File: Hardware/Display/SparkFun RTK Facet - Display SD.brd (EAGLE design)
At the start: 49 x 22 mm, 42 parts, among them J1 FPC_12_0.5MM_BACKFLIP, J2 MICRO-SD-PUSH-PUSH-EXT-PIN, J3 FPC_12_0.5MM_BACKFLIP, U13 LIS2DH12

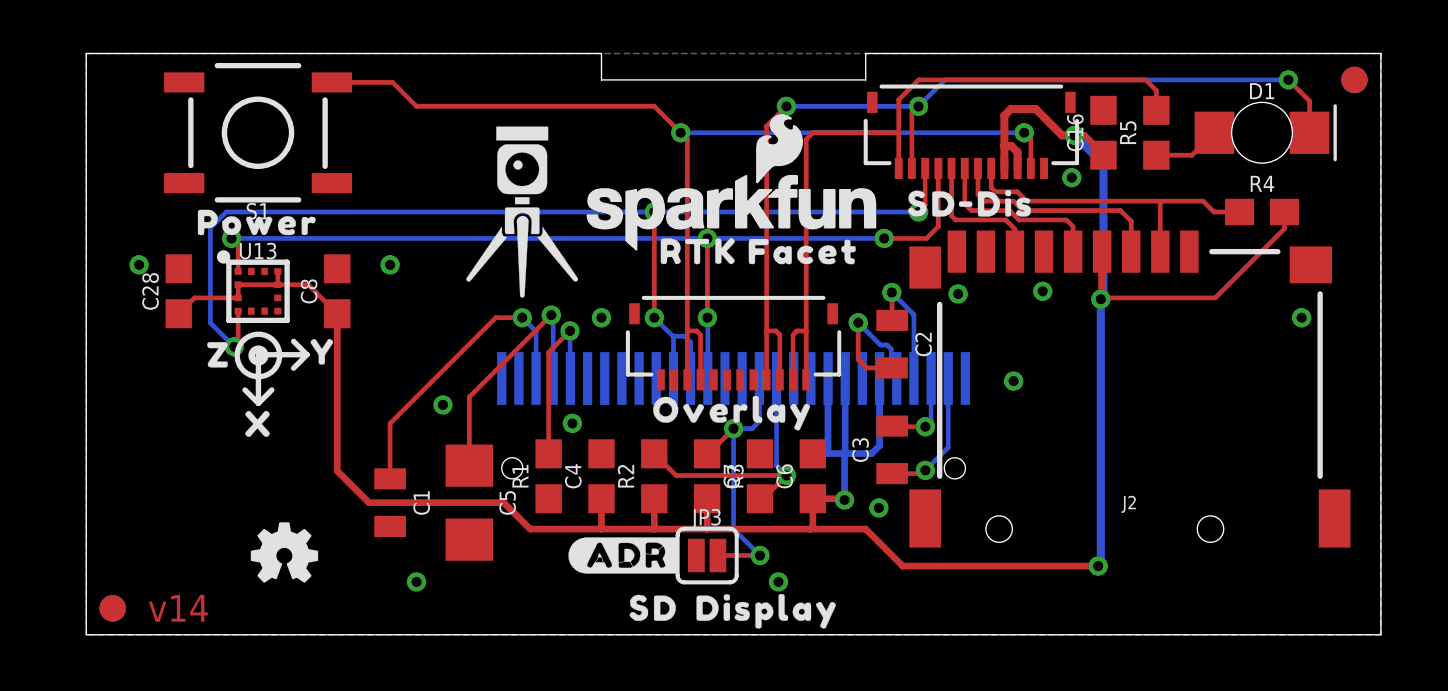
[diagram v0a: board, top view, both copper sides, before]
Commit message: Move to LIF overlay connector.
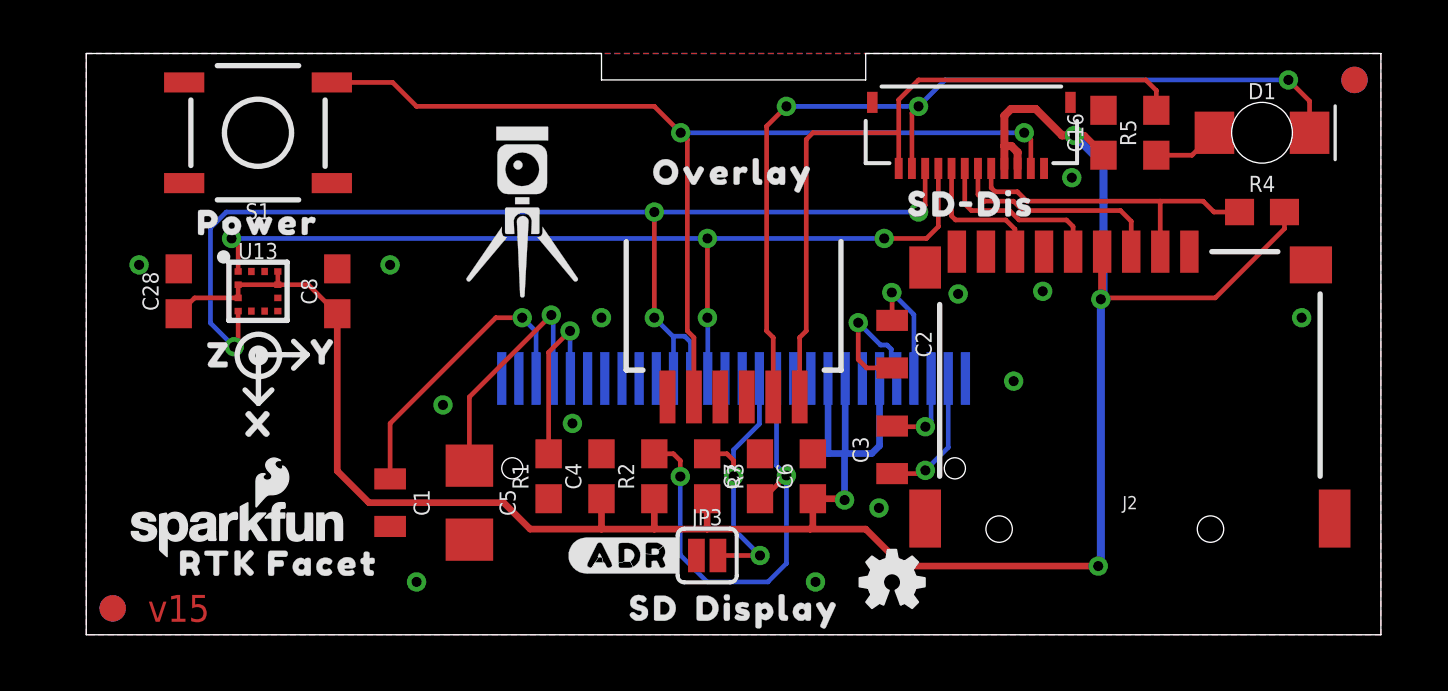
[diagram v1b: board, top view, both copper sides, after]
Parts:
- removed J3: FPC_12_0.5MM_BACKFLIP, RTK Facet:FPC_12_DOUBLESIDED_BACKFLIP
- added JP1: CONN_06, 1mm Pitch Connector:FPC_6_1MM-LIF
- added U$6: SPECIAL_INSTRUCTIONS-ORDERING, SparkFun-Aesthetics:ORDERING_INSTRUCTIONS
- LOGO5: value SFE_LOGO_NAME_FLAME.1_INCH -> SFE_LOGO_NAME_FLAME8_MM; device SparkFun-Aesthetics:SFE_LOGO_NAME_FLAME_.1 -> SparkFun-Aesthetics:SFE_LOGO_NAME_FLAME_8MM
- moved FRAME1 27.7 mm to (74.4, -12.5), flipped to the top
- moved LOGO3 23.0 mm to (30.5, 2.00)
- moved LOGO5 22.2 mm to (5.70, 4.10)
- moved U$13 21.7 mm to (7.30, 2.70)
- moved U$2 9.00 mm to (24.5, 17.5)
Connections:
- net CHARGE_LED: now also JP1.2; no longer J3.3, J3.4
- net GND: now also JP1.6; no longer J3.11, J3.12
- net POWER_BTN: now also JP1.5; no longer J3.10, J3.9
- net V_USB: now also JP1.1; no longer J3.1, J3.2
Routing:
- net RESET: track 10.5 -> 17.9 mm, vias 1 -> 2
- net V_USB: track 28.5 -> 27.0 mm
- net POWER_BTN: track 40.2 -> 38.7 mm
- net CHARGE_LED: track 37.1 -> 35.6 mm
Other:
- board text added: "2 Layer Board"
- board text added: "Board thickness is 1.6mm"
- board text added: "ENIG Finish"
- board text added: "v15"
- board text removed: "v14"

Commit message: Change to LIF 6 pin connector, remove GND plane around accel.
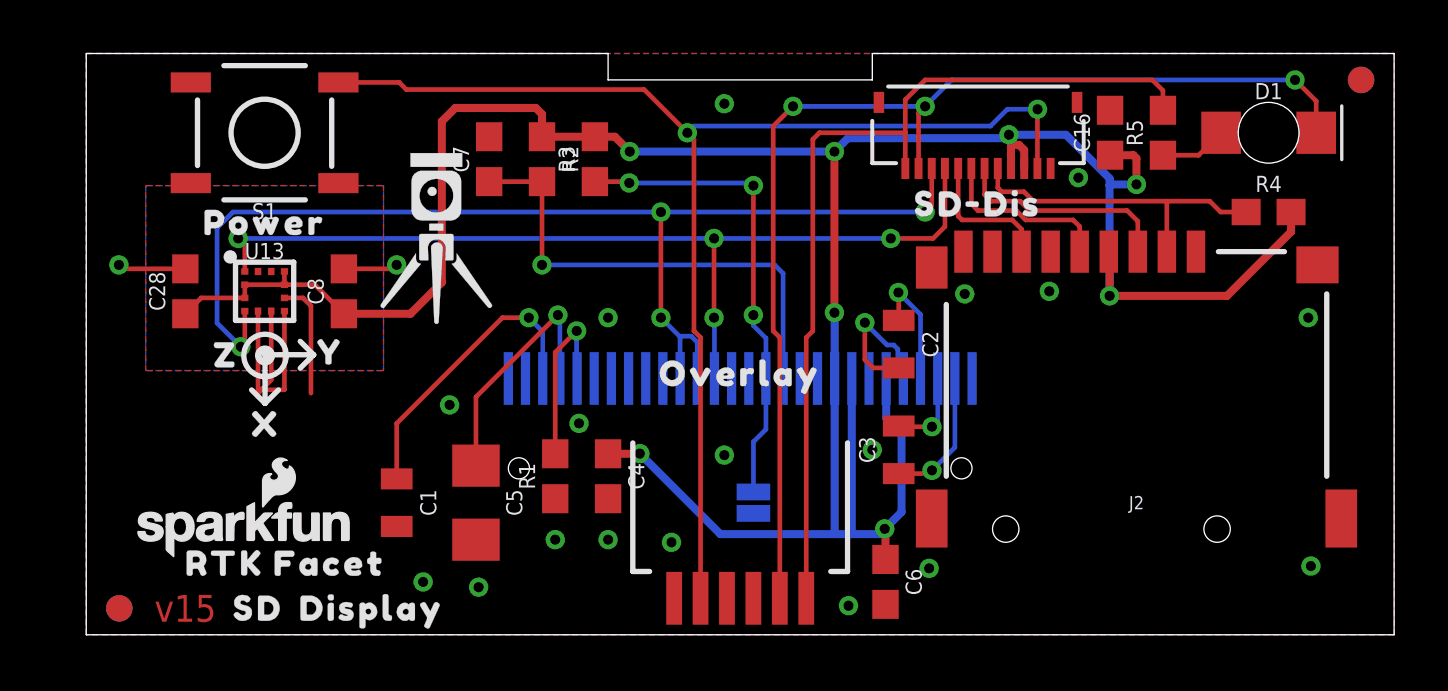
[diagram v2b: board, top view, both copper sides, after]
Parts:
- moved LOGO3 28.2 mm to (2.75, 7.00), flipped to the bottom
- moved C7 15.8 mm to (15.2, 18.0)
- moved U$3 15.0 mm to (10.8, 1.00)
- moved U$4 15.0 mm to (6.51, 1.00)
- moved R2 12.7 mm to (17.2, 18.0), turned to 270 degrees
- moved R3 12.7 mm to (19.2, 18.0), turned to 90 degrees
- moved U$7 8.00 mm to (28.2, 5.00), flipped to the bottom
- moved JP1 7.62 mm to (24.8, 4.38)
- moved U$2 7.62 mm to (24.8, 9.88)
- moved C6 4.85 mm to (30.2, 2.00), turned to 270 degrees
- moved U$5 3.40 mm to (13.2, 15.0)
- moved JP3 2.66 mm to (25.2, 5.00), flipped to the bottom, turned to 90 degrees
- moved C1 0.25 mm to (11.8, 5.00)
- moved C16 0.25 mm to (38.8, 19.0)
- moved C2 0.25 mm to (30.8, 11.0)
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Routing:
- net GND: track 0.00 -> 19.4 mm, vias 13 -> 20
- net POWER_BTN: track 38.7 -> 47.7 mm
- net 3.3V: track 97.0 -> 105.6 mm, vias 4 -> 8
- net V_USB: track 27.0 -> 34.7 mm
- net CHARGE_LED: track 35.6 -> 43.2 mm
- net D/C: track 10.8 -> 18.0 mm, vias 2 -> 3
- net RESET: track 17.9 -> 18.4 mm, vias 2 -> 1
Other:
- board size 49 x 22 mm -> 49.5 x 22 mm

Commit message: v15 panel files. Add tCream to LIF.
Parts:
- JP1: value CONN_06 -> (none); device 1mm Pitch Connector:FPC_6_1MM-LIF -> SparkFun-Connectors:FPC_6_1MM-LIF
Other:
- board text added: "Red Soldermask"
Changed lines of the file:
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@@
 <setting verticaltext="up"/>
 </settings>
-<grid distance="1" unitdist="mm" unit="mm" style="lines" multiple="1" display="yes" altdistance="0.25" altunitdist="mm" altunit="mm"/>
+<grid distance="0.05" unitdist="inch" unit="inch" style="lines" multiple="1" display="yes" altdistance="0.005" altunitdist="inch" altunit="inch"/>
 <layers>
 <layer number="1" name="Top/Vert" color="4" fill="1" visible="yes" active="yes"/>
@@
 <layer number="47" name="Measures" color="7" fill="1" visible="no" active="yes"/>
 <layer number="48" name="Document" color="7" fill="1" visible="no" active="yes"/>
-<layer number="49" name="Reference" color="7" fill="1" visible="yes" active="yes"/>
+<layer number="49" name="Reference" color="7" fill="1" visible="no" active="yes"/>
 <layer number="50" name="dxf" color="7" fill="1" visible="no" active="yes"/>
 <layer number="51" name="tDocu" color="6" fill="1" visible="yes" active="yes"/>
@@
 <text x="65" y="32.8" size="1.778" layer="51" font="vector" ratio="15">ENIG Finish</text>
 <text x="65" y="35.34" size="1.778" layer="51" font="vector" ratio="15">2 Layer Board</text>
+<text x="65" y="30.26" size="1.778" layer="51" font="vector" ratio="15">Red Soldermask</text>
 </plain>
 <attributes>
@@
 <attribute name="VALUE" x="39.75" y="4" size="0.5" layer="27" align="center"/>
 </element>
-<element name="JP1" library="1mm Pitch Connector" package="FPC_6_1MM-LIF" value="CONN_06" x="24.75" y="4.38" smashed="yes" rot="R180">
-<attribute name="DIGIKEY" value="PCB-C5-06-SA-SMT" x="24.75" y="4.38" size="1.778" layer="27" font="vector" ratio="15" rot="R180" display="off"/>
+<element name="JP1" library="SparkFun-Connectors" package="FPC_6_1MM-LIF" value="" x="24.75" y="4.38" smashed="yes" rot="R180">
+<attribute name="PROD_ID" value="CONN-16692" x="24.75" y="4.38" size="1.778" layer="27" rot="R180" display="off"/>
 </element>
 <element name="U$6" library="SparkFun-Aesthetics" package="ORDERING_INSTRUCTIONS" value="SPECIAL_INSTRUCTIONS-ORDERING" x="63.73" y="50.58" smashed="yes"/>

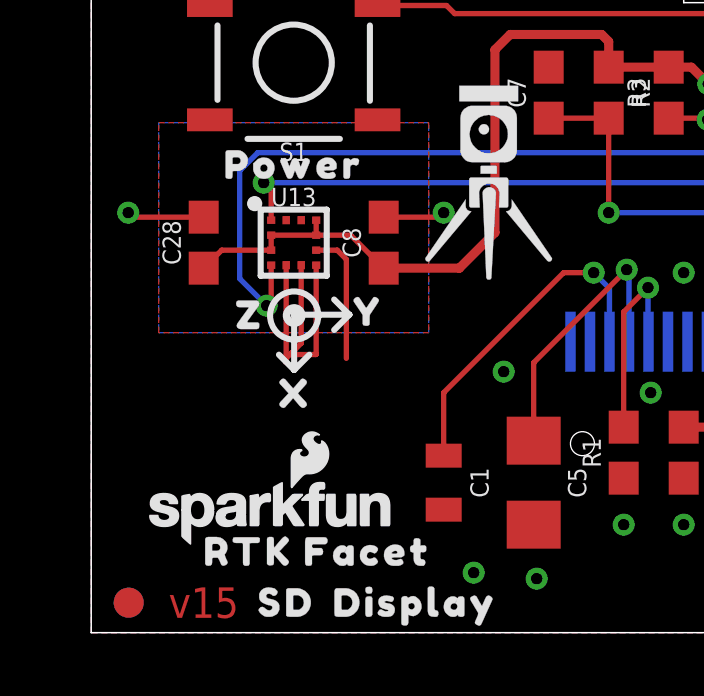
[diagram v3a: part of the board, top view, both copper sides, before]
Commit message: Add I2C test header to display board - v1.6
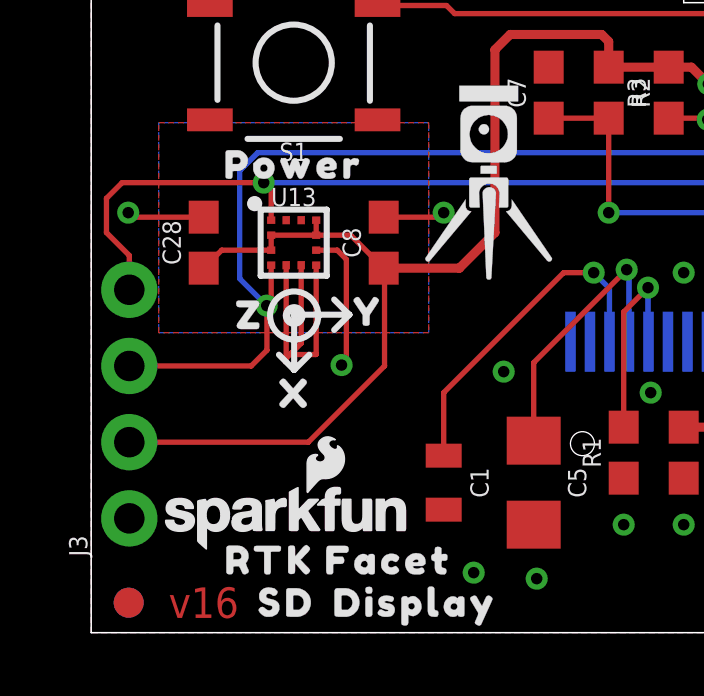
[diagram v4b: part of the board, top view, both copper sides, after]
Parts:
- added J3: (no value), SparkFun-Connectors:1X04_NO_SILK
- added U$14: (no value), output:3V33
- added U$15: (no value), output:GND2
- added U$16: (no value), output:SCL0
- added U$17: (no value), output:SDA1
- moved LOGO3 7.41 mm to (9.10, 3.19)
- moved U$13 0.76 mm to (8.26, 2.41)
- moved LOGO5 0.55 mm to (6.48, 3.94)
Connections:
- net 3.3V: now also J3.2
- net ESP_21/SDA: now also J3.3
- net ESP_22/SCL: now also J3.4
- net GND: now also J3.1
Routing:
- net 3.3V: track 105.6 -> 118.4 mm
- net ESP_22/SCL: track 35.8 -> 44.6 mm
- net ESP_21/SDA: track 43.8 -> 50.1 mm
- net GND: vias 20 -> 21
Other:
- board text added: "v16"
- board text removed: "v15"
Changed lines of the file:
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@@
 <board>
 <plain>
-<text x="3.75" y="1" size="1.016" layer="1" font="vector" ratio="20" rot="R180" align="center">v15</text>
+<text x="3.75" y="1" size="1.016" layer="1" font="vector" ratio="20" rot="R180" align="center">v16</text>
 <wire x1="0" y1="0" x2="0" y2="22" width="0.05" layer="20"/>
 <wire x1="49.5" y1="22" x2="49.5" y2="0" width="0.05" layer="20"/>
@@
 <attribute name="VALUE" x="29.488" y="2" size="0.6096" layer="27" font="vector" ratio="20" rot="R270" align="top-center"/>
 </element>
-<element name="LOGO3" library="SparkFun-Aesthetics" package="OSHW-LOGO-MINI" value="OSHW-LOGOMINI" x="2.75" y="7" smashed="yes" rot="MR0"/>
+<element name="LOGO3" library="SparkFun-Aesthetics" package="OSHW-LOGO-MINI" value="OSHW-LOGOMINI" x="9.1" y="3.19" smashed="yes" rot="MR0"/>
 <element name="R3" library="SparkFun-Resistors" package="0603" value="10k" x="19.25" y="18" smashed="yes" rot="R90">
 <attribute name="NAME" x="18.488" y="18" size="0.6096" layer="25" font="vector" ratio="20" rot="R90" align="bottom-center"/>
@@
 <attribute name="VALUE" x="44.75" y="15.238" size="0.6096" layer="27" font="vector" ratio="20" align="top-center"/>
 </element>
-<element name="LOGO5" library="SparkFun-Aesthetics" package="SFE_LOGO_NAME_FLAME_8MM" value="SFE_LOGO_NAME_FLAME8_MM" x="5.95" y="4.1" smashed="yes"/>
+<element name="LOGO5" library="SparkFun-Aesthetics" package="SFE_LOGO_NAME_FLAME_8MM" value="SFE_LOGO_NAME_FLAME8_MM" x="6.477" y="3.937" smashed="yes"/>
 <element name="U$3" library="output" package="DISPLAY0" value="" x="10.81" y="1" smashed="yes"/>
 <element name="U$4" library="output" package="SD1" value="" x="6.51" y="1" smashed="yes"/>
@@
 <element name="U$11" library="output" package="Y1" value="" x="9.25" y="10.7" smashed="yes"/>
 <element name="U$12" library="output" package="Z2" value="" x="5.15" y="10.6" smashed="yes" rot="R180"/>
-<element name="U$13" library="output" package="RTK_FACET0" value="" x="7.55" y="2.7" smashed="yes"/>
+<element name="U$13" library="output" package="RTK_FACET0" value="" x="8.255" y="2.413" smashed="yes"/>
 <element name="U$5" library="output" package="RTK5#SVG0" value="" x="13.25" y="15" smashed="yes"/>
 <element name="J2" library="SparkFun-Connectors" package="MICROSD-EXTERNALPIN" value="MICRO-SD-PUSH-PUSH-EXT-PIN" x="39.75" y="4" smashed="yes">
@@
 </element>
 <element name="U$6" library="SparkFun-Aesthetics" package="ORDERING_INSTRUCTIONS" value="SPECIAL_INSTRUCTIONS-ORDERING" x="63.73" y="50.58" smashed="yes"/>
+<element name="J3" library="SparkFun-Connectors" package="1X04_NO_SILK" value="" x="1.27" y="3.81" smashed="yes" rot="R90">
+<attribute name="NAME" x="-0.127" y="2.54" size="0.6096" layer="25" font="vector" ratio="20" rot="R90"/>
+<attribute name="VALUE" x="3.302" y="2.54" size="0.6096" layer="27" font="vector" ratio="20" rot="R90"/>
+</element>
+<element name="U$14" library="output" package="3V33" value="" x="3.81" y="6.35" smashed="yes" rot="MR0"/>
+<element name="U$15" library="output" package="GND2" value="" x="3.81" y="3.81" smashed="yes" rot="MR0"/>
+<element name="U$16" library="output" package="SCL0" value="" x="3.81" y="11.43" smashed="yes" rot="MR0"/>
+<element name="U$17" library="output" package="SDA1" value="" x="3.81" y="8.89" smashed="yes" rot="MR0"/>
 </elements>
 <signals>
@@
 <via x="24.15" y="6.8" extent="1-16" drill="0.381"/>
 <via x="24.15" y="20.1" extent="1-16" drill="0.381"/>
+<contactref element="J3" pad="1"/>
+<via x="8.346" y="8.92" extent="1-16" drill="0.381"/>
 </signal>
 <signal name="VCOMH">
@@
 <wire x1="28.952" y1="3.81" x2="30.022" y2="3.81" width="0.3048" layer="16"/>
 <wire x1="30.022" y1="3.81" x2="30.222" y2="4.01" width="0.3048" layer="16"/>
+<contactref element="J3" pad="2"/>
+<wire x1="1.27" y1="6.35" x2="7.239" y2="6.35" width="0.1778" layer="1"/>
+<wire x1="7.239" y1="6.35" x2="9.779" y2="8.89" width="0.1778" layer="1"/>
+<wire x1="9.779" y1="8.89" x2="9.779" y2="12.121" width="0.1778" layer="1"/>
+<wire x1="9.779" y1="12.121" x2="9.75" y2="12.15" width="0.1778" layer="1"/>
 </signal>
 <signal name="SD_!CS!">
@@
 <wire x1="6" y1="13.75" x2="6" y2="14.75" width="0.1778" layer="1"/>
 <wire x1="6" y1="14.75" x2="5.75" y2="15" width="0.1778" layer="1"/>
+<contactref element="J3" pad="4"/>
+<wire x1="1.27" y1="11.43" x2="1.27" y2="12.573" width="0.1778" layer="1"/>
+<wire x1="1.27" y1="12.573" x2="0.508" y2="13.335" width="0.1778" layer="1"/>
+<wire x1="0.508" y1="13.335" x2="0.508" y2="14.478" width="0.1778" layer="1"/>
+<wire x1="1.03" y1="15" x2="5.75" y2="15" width="0.1778" layer="1"/>
+<wire x1="0.508" y1="14.478" x2="1.03" y2="15" width="0.1778" layer="1"/>
 </signal>
 <signal name="ESP_21/SDA">
@@
 <via x="5.85" y="10.9" extent="1-16" drill="0.381"/>
 <wire x1="6" y1="12.25" x2="6" y2="11.05" width="0.1778" layer="1"/>
-<wire x1="6" y1="11.05" x2="5.85" y2="10.9" width="0.1778" layer="1"/>
+<wire x1="6" y1="11.05" x2="5.857" y2="10.907" width="0.1778" layer="1"/>
+<contactref element="J3" pad="3"/>
+<wire x1="5.857" y1="10.907" x2="5.85" y2="10.9" width="0.1778" layer="1"/>
+<wire x1="1.27" y1="8.89" x2="5.334" y2="8.89" width="0.1778" layer="1"/>
+<wire x1="5.334" y1="8.89" x2="5.857" y2="9.413" width="0.1778" layer="1"/>
+<wire x1="5.857" y1="9.413" x2="5.857" y2="10.907" width="0.1778" layer="1"/>
 </signal>
 <signal name="POWER_BTN">
